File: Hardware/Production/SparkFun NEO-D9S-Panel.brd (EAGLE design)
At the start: 160.8 x 107.4 mm, 672 parts, among them J1 ANTENNA-SMA-GROUNDEDEDGE_SMA, J11 ANTENNA-SMA-GROUNDEDEDGE_SMA, J15 Qwiic Right Angle, J16 Qwiic Right Angle, J18 ANTENNA-SMA-GROUNDEDEDGE_SMA, J2 Qwiic Right Angle, J22 Qwiic Right Angle, J23 Qwiic Right Angle, J25 ANTENNA-SMA-GROUNDEDEDGE_SMA, J29 Qwiic Right Angle, J30 Qwiic Right Angle, J32 ANTENNA-SMA-GROUNDEDEDGE_SMA, J36 Qwiic Right Angle, J37 Qwiic Right Angle, J39 ANTENNA-SMA-GROUNDEDEDGE_SMA, J4 Qwiic Right Angle, J6 Qwiic Right Angle, J9 Qwiic Right Angle, U1 U-BLOX_NEO-D9S-00B, U10 U-BLOX_NEO-D9S-00B, U11 3.3V, U12 U-BLOX_NEO-D9S-00B, U2 3.3V, U3 3.3V, U4 U-BLOX_NEO-D9S-00B, U5 3.3V, U6 U-BLOX_NEO-D9S-00B, U7 3.3V, U8 U-BLOX_NEO-D9S-00B, U9 3.3V

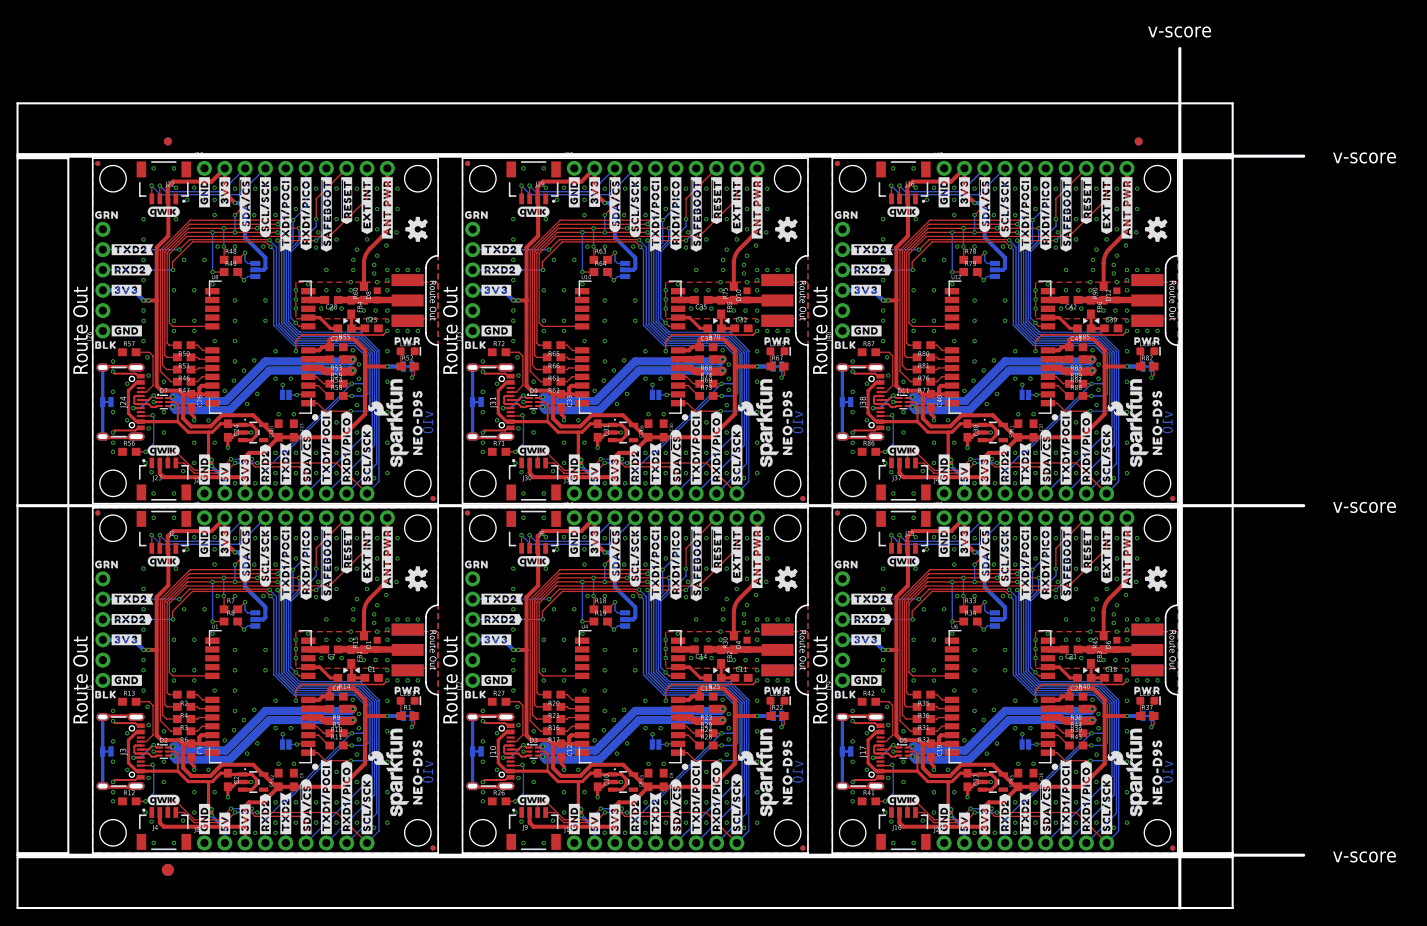
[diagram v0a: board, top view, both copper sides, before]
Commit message: Updates after REDs Review
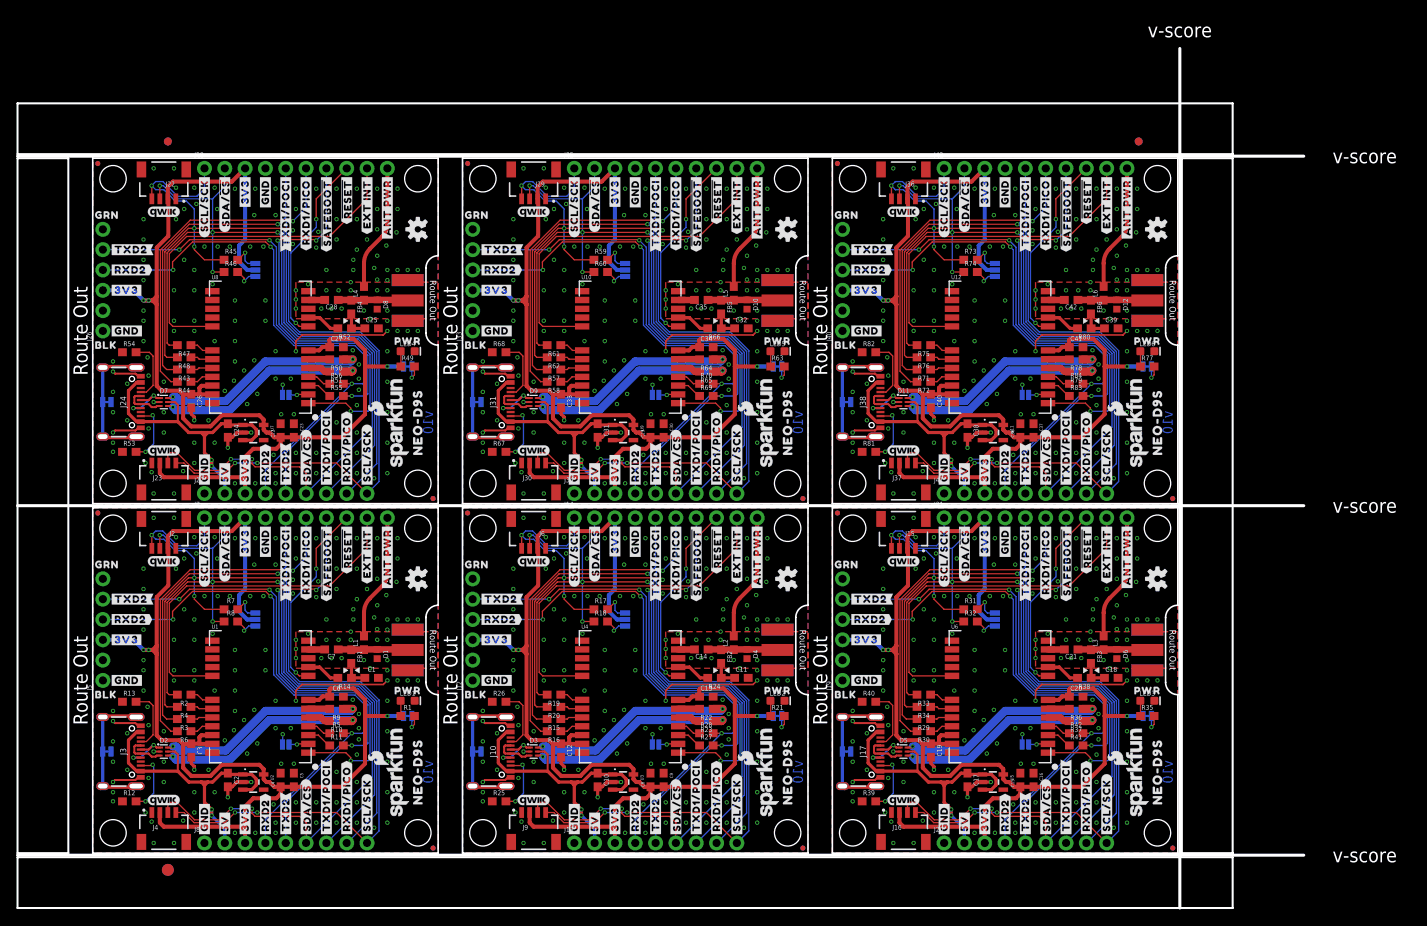
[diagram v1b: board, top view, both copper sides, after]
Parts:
- removed R85: 10, SparkFun-Resistors:0603
- removed R86, R87: 5.1k, SparkFun-Resistors:0603
- removed R88, R89: 33, SparkFun-Resistors:0603
- removed R90: DNP, SparkFun-Resistors:0603_NO_CREAM
- added L1, L2, L3, L4, L5, L6: DNP, SparkFun-Coils:0603_NO-CREAM
- R15, R30, R75: value DNP -> 33; device SparkFun-Resistors:0603_NO_CREAM -> SparkFun-Resistors:0603
- R17, R31, R32, R46, R59, R73, R74: value 33 -> 2.2k
- R19, R33, R34, R48: value 2.2k -> 33
- R21, R35, R77: value 33 -> 1k
- R22, R37: value 1k -> 27
- R24, R38: value 27 -> 10
- R25, R40: value 10 -> 5.1k
- R27, R41, R42, R56, R57, R71, R72: value 5.1k -> 33
- R36, R50, R51, R65: value 33 -> 27
- R39, R53, R54, R68: value 27 -> 5.1k
- R45, R60: value DNP -> 2.2k; device SparkFun-Resistors:0603_NO_CREAM -> SparkFun-Resistors:0603
- R49, R63: value 2.2k -> 1k
- R52: value 1k -> 10
- R55, R70: value 10 -> 33
- R64, R78, R79: value 2.2k -> 27
- R66, R80: value 33 -> 10
- R67, R82: value 1k -> 5.1k
- R69, R83, R84: value 27 -> 33
- R81: value 33 -> 5.1k
- moved R43 121.0 mm to (11.4, 60.5), turned to 180 degrees
- moved R44 119.9 mm to (11.4, 58.9), turned to 180 degrees
- moved R45 119.1 mm to (17.3, 74.2), turned to 0 degrees
- moved R71 54.1 mm to (103.9, 60.5), turned to 180 degrees
- moved R72 53.2 mm to (103.9, 58.9), turned to 180 degrees
- moved R57 53.1 mm to (57.7, 60.5), turned to 180 degrees
- moved R73 37.1 mm to (109.7, 74.2)
- moved R59 36.5 mm to (63.5, 74.2)
- moved R67 36.4 mm to (50.8, 50.2)
- moved R74 35.9 mm to (109.7, 72.6)
- moved R82 34.8 mm to (97.0, 62.6)
- moved R25 31.0 mm to (50.8, 6.48), turned to 0 degrees
- moved R60 29.7 mm to (63.5, 72.6), turned to 0 degrees
- moved R53 28.4 mm to (4.57, 50.2), turned to 0 degrees
- moved R35 28.1 mm to (131.8, 17.1), turned to 0 degrees
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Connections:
- net 3.3V: now also J7.3; no longer J7.2
- net 3.3V1: now also J14.3; no longer J14.2
- net 3.3V2: now also J21.3; no longer J21.2
- net 3.3V3: now also J28.3; no longer J28.2
- net 3.3V4: now also J35.3; no longer J35.2
- net 3.3V5: now also J42.3; no longer J42.2
- net ANT_PWR: now also L1.2; no longer R15.2
- net ANT_PWR1: now also L2.2; no longer R30.2
- net ANT_PWR2: now also L3.2; no longer R45.2
- net ANT_PWR3: now also L4.2; no longer R60.2
- net ANT_PWR4: now also L5.2; no longer R75.2
- net ANT_PWR5: now also L6.2; no longer R90.2
- net ANT_VCC1: now also R24.1; no longer R25.1
- net ANT_VCC2: now also R38.1; no longer R40.1
- net ANT_VCC3: now also R52.1; no longer R55.1
- net ANT_VCC4: now also R66.1; no longer R70.1
- net ANT_VCC5: now also R80.1; no longer R85.1
- net D+1: now also R22.1; no longer R23.1
- net D+2: now also R36.1; no longer R38.1
- net D+3: now also R50.1; no longer R53.1
- net D+4: now also R64.1; no longer R68.1
- net D+5: now also R78.1; no longer R83.1
- net D-1: now also R23.1; no longer R24.1
- net D-2: now also R37.1; no longer R39.1
- net D-3: now also R51.1; no longer R54.1
- net D-4: now also R65.1; no longer R69.1
- net D-5: now also R79.1; no longer R84.1
- net GND: now also J7.4; no longer J7.1
- net GND1: now also J14.4, R25.1; no longer J14.1, R27.1
- net GND2: now also J21.4, R39.1, R40.1; no longer J21.1, R41.1, R42.1
- net GND3: now also J28.4, R53.1, R54.1; no longer J28.1, R56.1, R57.1
- net GND4: now also J35.4, R67.1, R68.1; no longer J35.1, R71.1, R72.1
- net GND5: now also J42.4, R81.1, R82.1; no longer J42.1, R86.1, R87.1
- net N$16: now also R18.2; no longer R19.2
- net N$17: now also R17.2; no longer R18.2
- net N$18: now also R21.1; no longer R22.1
- net N$19: now also R22.2; no longer R23.2
- net N$20: now also R23.2; no longer R24.2
- net N$21: now also R21.2; no longer R22.2
- net N$22: now also R25.2; no longer R26.2
- net N$23: now also R26.2; no longer R27.2
- net N$24: now also R27.1; no longer R28.1
- net N$25: now also R28.1; no longer R29.1
- net N$26: now also R15.1; no longer R16.1
- net N$27: now also R16.1; no longer R17.1
- net N$28: now also R19.1; no longer R20.1
- net N$29: now also R20.1; no longer R21.1
- net N$31: now also R32.2; no longer R34.2
- net N$32: now also R31.2; no longer R33.2
- net N$33: now also R35.1; no longer R37.1
- net N$34: now also R36.2; no longer R38.2
- net N$35: now also R37.2; no longer R39.2
- net N$36: now also R35.2; no longer R37.2
- net N$37: now also R39.2; no longer R41.2
- net N$38: now also R40.2; no longer R42.2
- net N$39: now also R41.1; no longer R43.1
- net N$40: now also R42.1; no longer R44.1
- net N$41: now also R29.1; no longer R31.1
- net N$42: now also R30.1; no longer R32.1
- net N$43: now also R33.1; no longer R35.1
- net N$44: now also R34.1; no longer R36.1
- net N$46: now also R46.2; no longer R49.2
- net N$47: now also R45.2; no longer R48.2
- net N$48: now also R49.1; no longer R52.1
- net N$49: now also R50.2; no longer R53.2
- net N$50: now also R51.2; no longer R54.2
- net N$51: now also R49.2; no longer R52.2
- net N$52: now also R53.2; no longer R56.2
- net N$53: now also R54.2; no longer R57.2
- net N$54: now also R55.1; no longer R58.1
- net N$55: now also R56.1; no longer R59.1
- net N$56: now also R43.1; no longer R46.1
- net N$57: now also R44.1; no longer R47.1
- net N$58: now also R47.1; no longer R50.1
- net N$59: now also R48.1; no longer R51.1
- net N$61: now also R60.2; no longer R64.2
- net N$62: now also R59.2; no longer R63.2
- net N$63: now also R63.1; no longer R67.1
- net N$64: now also R64.2; no longer R68.2
- net N$65: now also R65.2; no longer R69.2
- net N$66: now also R63.2; no longer R67.2
- net N$67: now also R67.2; no longer R71.2
- net N$68: now also R68.2; no longer R72.2
- net N$69: now also R69.1; no longer R73.1
- net N$70: now also R70.1; no longer R74.1
- net N$71: now also R57.1; no longer R61.1
- net N$72: now also R58.1; no longer R62.1
- net N$73: now also R61.1; no longer R65.1
- net N$74: now also R62.1; no longer R66.1
- net N$76: now also R74.2; no longer R79.2
- net N$77: now also R73.2; no longer R78.2
- net N$78: now also R77.1; no longer R82.1
- net N$79: now also R78.2; no longer R83.2
- net N$80: now also R79.2; no longer R84.2
- net N$81: now also R77.2; no longer R82.2
- net N$82: now also R81.2; no longer R86.2
- net N$83: now also R82.2; no longer R87.2
- net N$84: now also R83.1; no longer R88.1
- net N$85: now also R84.1; no longer R89.1
- net N$86: now also R71.1; no longer R76.1
- net N$87: now also R72.1; no longer R77.1
- net N$88: now also R75.1; no longer R80.1
- net N$89: now also R76.1; no longer R81.1
- net RXD1: now also R28.2; no longer R29.2
- net RXD1/PICO1: now also R16.2; no longer R17.2
- net RXD1/PICO2: now also R30.2; no longer R32.2
- net RXD1/PICO3: now also R44.2; no longer R47.2
- net RXD1/PICO4: now also R58.2; no longer R62.2
- net RXD1/PICO5: now also R72.2; no longer R77.2
- net RXD3: now also R42.2; no longer R44.2
- net RXD4: now also R56.2; no longer R59.2
- net RXD5: now also R70.2; no longer R74.2
- net RXD6: now also R84.2; no longer R89.2
- net SCL/SCK: now also J7.1; no longer J7.4
- net SCL/SCK1: now also J14.1, R17.1, R20.2; no longer J14.4, R18.1, R21.2
- net SCL/SCK2: now also J21.1, R31.1, R34.2; no longer J21.4, R33.1, R36.2
- net SCL/SCK3: now also J28.1, R45.1, R48.2; no longer J28.4, R48.1, R51.2
- net SCL/SCK4: now also J35.1, R59.1, R62.2; no longer J35.4, R63.1, R66.2
- net SCL/SCK5: now also J42.1, R73.1, R76.2; no longer J42.4, R78.1, R81.2
- net SDA/!CS!: now also J7.2; no longer J7.3
- net SDA/!CS!1: now also J14.2, R18.1, R19.2; no longer J14.3, R19.1, R20.2
- net SDA/!CS!2: now also J21.2, R32.1, R33.2; no longer J21.3, R34.1, R35.2
- net SDA/!CS!3: now also J28.2, R46.1, R47.2; no longer J28.3, R49.1, R50.2
- net SDA/!CS!4: now also J35.2, R60.1, R61.2; no longer J35.3, R64.1, R65.2
- net SDA/!CS!5: now also J42.2, R74.1, R75.2; no longer J42.3, R79.1, R80.2
- net SMA: now also L1.1; no longer R15.1
- net SMA1: now also L2.1; no longer R30.1
- net SMA2: now also L3.1; no longer R45.1
- net SMA3: now also L4.1; no longer R60.1
- net SMA4: now also L5.1; no longer R75.1
- net SMA5: now also L6.1; no longer R90.1
- net TXD1: now also R27.2; no longer R28.2
- net TXD1/POCI1: now also R15.2; no longer R16.2
- net TXD1/POCI2: now also R29.2; no longer R31.2
- net TXD1/POCI3: now also R43.2; no longer R46.2
- net TXD1/POCI4: now also R57.2; no longer R61.2
- net TXD1/POCI5: now also R71.2; no longer R76.2
- net TXD3: now also R41.2; no longer R43.2
- net TXD4: now also R55.2; no longer R58.2
- net TXD5: now also R69.2; no longer R73.2
- net TXD6: now also R83.2; no longer R88.2
- net VCC_RF1: now also R24.2; no longer R25.2
- net VCC_RF2: now also R38.2; no longer R40.2
- net VCC_RF3: now also R52.2; no longer R55.2
- net VCC_RF4: now also R66.2; no longer R70.2
- net VCC_RF5: now also R80.2; no longer R85.2
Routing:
- net SDA/!CS!1: track 125.2 -> 120.4 mm, vias 8 -> 6
- net SDA/!CS!5: track 125.2 -> 120.4 mm, vias 8 -> 6
- net SDA/!CS!4: track 125.2 -> 120.4 mm, vias 8 -> 6
- net SDA/!CS!3: track 125.2 -> 120.4 mm, vias 8 -> 6
- net SDA/!CS!2: track 125.2 -> 120.4 mm, vias 8 -> 6
- net SDA/!CS!: track 125.2 -> 120.4 mm, vias 8 -> 6
- net 3.3V1: track 137.2 -> 141.4 mm, vias 4 -> 3
- net 3.3V5: track 137.2 -> 141.4 mm, vias 4 -> 3
- net 3.3V3: track 137.2 -> 141.4 mm, vias 4 -> 3
- net 3.3V: track 137.2 -> 141.4 mm, vias 4 -> 3
- net 3.3V2: track 137.2 -> 141.4 mm, vias 4 -> 3
- net 3.3V4: track 137.2 -> 141.4 mm, vias 4 -> 3
- net SCL/SCK2: track 132.2 -> 129.4 mm, vias 7 -> 6
- net SCL/SCK1: track 132.2 -> 129.4 mm, vias 7 -> 6
- net SCL/SCK3: track 132.2 -> 129.4 mm, vias 7 -> 6
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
